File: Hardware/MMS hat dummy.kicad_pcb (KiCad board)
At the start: 2 copper layers, 100 x 20 mm, 26 parts, among them J1 Chainbus in, J2 Chainbus Out, U1 XC6206P332MR

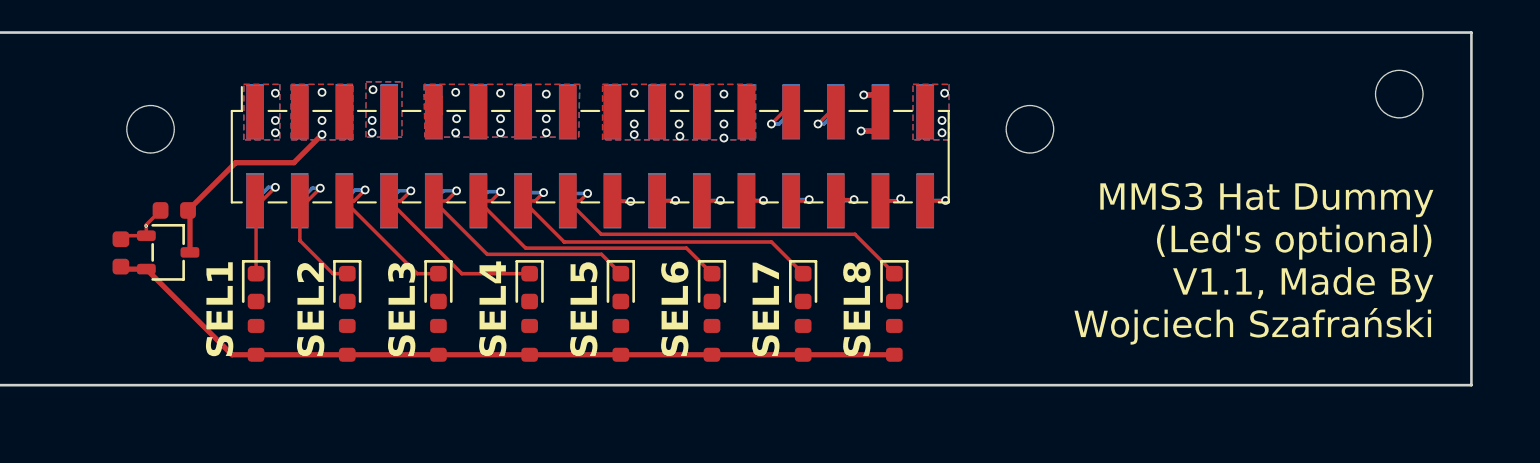
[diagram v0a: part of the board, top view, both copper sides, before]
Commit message: MAJOR - fixed DIN holes misalignment
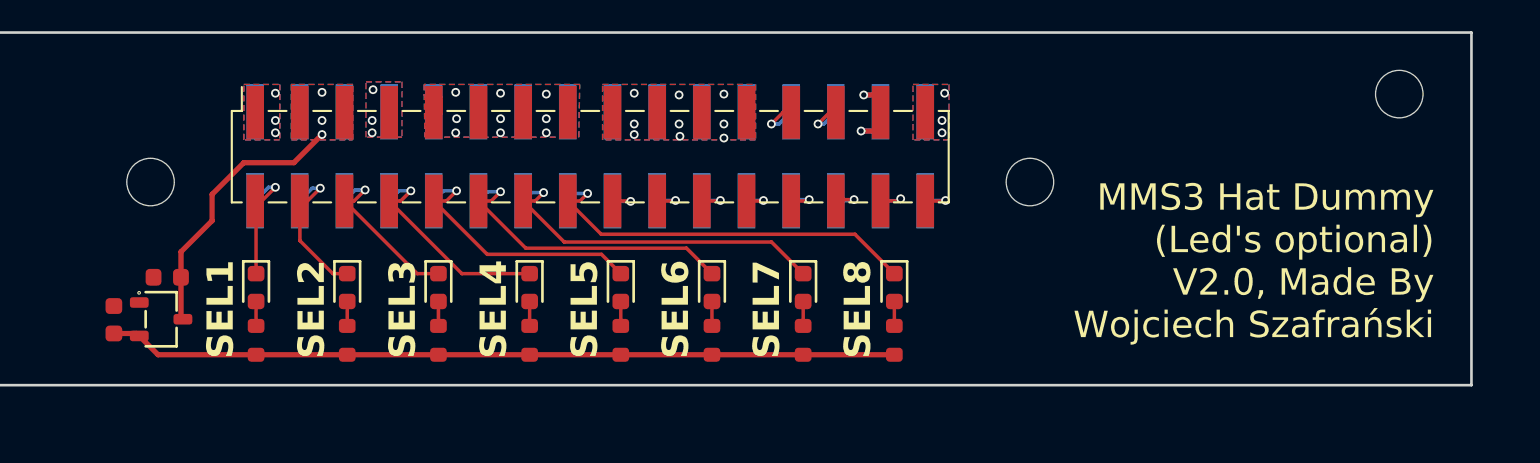
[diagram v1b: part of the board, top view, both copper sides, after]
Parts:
- moved C1 3.82 mm to (104.0, 102.4)
- moved C2 3.82 mm to (100.9, 104.8)
- moved U1 3.82 mm to (103.6, 104.8)
- moved H5 3.00 mm to (103.0, 97.0)
- moved H6 3.00 mm to (153.0, 97.0)
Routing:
- net +5V: track 11.8 -> 15.5 mm
- net GND: track 3.30 -> 0.00 mm
- net Net-(D8-Pad2): track 0.00 -> 1.39 mm
- net Net-(D7-Pad2): track 0.00 -> 1.39 mm
- net Net-(D6-Pad2): track 0.00 -> 1.39 mm
- net Net-(D5-Pad2): track 0.00 -> 1.39 mm
- net Net-(D4-Pad2): track 0.00 -> 1.39 mm
- net Net-(D3-Pad2): track 0.00 -> 1.39 mm
- net Net-(D2-Pad2): track 0.00 -> 1.39 mm
- net Net-(D1-Pad2): track 0.00 -> 1.39 mm
- net +3V3: track 46.1 -> 44.9 mm
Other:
- board text added: "MMS3 Hat Dummy (Led's optional) V2.0, Made By Wojciech Szafrański"
- board text removed: "MMS3 Hat Dummy (Led's optional) V1.1, Made By Wojciech Szafrański"
- board text removed: "i"
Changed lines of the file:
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@@
 	(title_block
 		(title "MMS hat dummy")
-		(date "2026-06-23")
-		(rev "Ver 1.0")
+		(date "2026-10-19")
+		(rev "2.0")
 		(comment 1 "Made by Wojciech Szafrański")
 		(comment 2 "Designed in poland")
@@
 	(footprint "PCM_JLCPCB:C_0603"
 		(layer "F.Cu")
-		(at 104.35 98.615 180)
+		(at 103.95 102.415 180)
 		(descr "Capacitor SMD 0603 (1608 Metric), square (rectangular) end terminal, IPC_7351 nominal, (Body size source: IPC-SM-782 page 76, https://www.pcb-3d.com/wordpress/wp-content/uploads/ipc-sm-782a_amendment_1_and_2.pdf), generated with kicad-footprint-generator")
 		(tags "capacitor")
@@
 	(footprint "PCM_JLCPCB:SOT-23-3_L2.9-W1.6-P1.90-LS2.8-BR"
 		(layer "F.Cu")
-		(at 104 101 180)
+		(at 103.6 104.8 180)
 		(descr "SOT-23-3_L2.9-W1.6-P1.90-LS2.8-BR footprint")
 		(tags "SOT-23-3_L2.9-W1.6-P1.90-LS2.8-BR footprint C2829399")
@@
 		(locked yes)
 		(layer "F.Cu")
-		(at 153 94)
+		(at 153 97)
 		(descr "Mounting Hole 2.7mm, M2.5, no annular, generated by kicad-footprint-generator mountinghole.py")
 		(tags "mountinghole M2.5")
@@
 		(locked yes)
 		(layer "F.Cu")
-		(at 103 94)
+		(at 103 97)
 		(descr "Mounting Hole 2.7mm, M2.5, no annular, generated by kicad-footprint-generator mountinghole.py")
 		(tags "mountinghole M2.5")
@@
 	(footprint "PCM_JLCPCB:C_0603"
 		(layer "F.Cu")
-		(at 101.314826 101.030476 90)
+		(at 100.914826 104.830476 90)
 		(descr "Capacitor SMD 0603 (1608 Metric), square (rectangular) end terminal, IPC_7351 nominal, (Body size source: IPC-SM-782 page 76, https://www.pcb-3d.com/wordpress/wp-content/uploads/ipc-sm-782a_amendment_1_and_2.pdf), generated with kicad-footprint-generator")
 		(tags "capacitor")
@@
 		(layer "Edge.Cuts")
 	)
-	(gr_text "MMS3 Hat Dummy\n(Led's optional)\nV1.1, Made By\nWojciech Szafrański"
+	(gr_text "MMS3 Hat Dummy\n(Led's optional)\nV2.0, Made By\nWojciech Szafrański"
 		(at 176 106 0)
 		(layer "F.SilkS")
@@
 		)
 	)
-	(gr_text "i"
-		(at 157.776979 93.689038 0)
-		(layer "B.SilkS")
-		(effects
-			(font
-				(face "Microsoft Himalaya")
-				(size 3 3)
-				(thickness 0.4)
-				(bold yes)
-			)
-			(justify left bottom mirror)
-		)
-		(render_cache "i" 0
-			(polygon
-				(pts
-					(xy 157.147015 89.982876) (xy 157.015354 89.999715) (xy 156.905581 90.048088) (xy 156.851273 90.100029)
-					(xy 156.816027 90.1784) (xy 156.802633 90.293553) (xy 156.815759 90.403246) (xy 156.850792 90.48016)
-					(xy 156.905581 90.533155) (xy 157.015476 90.582921) (xy 157.147015 90.600199) (xy 157.281779 90.58274)
-					(xy 157.390647 90.533155) (xy 157.444135 90.480351) (xy 157.478493 90.403468) (xy 157.491398 90.293553)
-					(xy 157.478227 90.178165) (xy 157.44366 90.099831) (xy 157.390647 90.048088) (xy 157.281907 89.999893)
-				)
-			)
-			(polygon
-				(pts
-					(xy 156.831942 90.88578) (xy 156.831942 93.179038) (xy 157.466118 93.179038) (xy 157.466118 90.88578)
-				)
-			)
-		)
-	)
 	(gr_text "Front and Back keepout\nzone for DIN rail mount"
 		(locked yes)
@@
 	(dimension
 		(type orthogonal)
-		(locked yes)
 		(layer "User.1")
 		(pts
-			(xy 153 94) (xy 178 88)
+			(xy 153 97) (xy 178 88)
 		)
 		(height 34)
@@
 			(keep_text_aligned yes)
 		)
-		(gr_text "6"
-			(locked yes)
-			(at 185.85 91 90)
+		(gr_text "9"
+			(at 185.85 92.5 90)
 			(layer "User.1")
 			(effects
@@
 	)
 	(segment
-		(start 102.76 101.95)
-		(end 101.45435 101.95)
+		(start 109 106.82)
+		(end 103.43 106.82)
 		(width 0.3)
 		(layer "F.Cu")
@@
 	)
 	(segment
-		(start 107.63 106.82)
-		(end 102.76 101.95)
+		(start 109 106.82)
+		(end 145.29 106.82)
 		(width 0.3)
 		(layer "F.Cu")
@@
 	)
 	(segment
-		(start 101.45435 101.95)
-		(end 101.314826 101.810476)
+		(start 100.914826 105.610476)
+		(end 102.220476 105.610476)
 		(width 0.3)
 		(layer "F.Cu")
@@
 	)
 	(segment
-		(start 107.63 106.82)
-		(end 145.29 106.82)
+		(start 102.220476 105.610476)
+		(end 102.36 105.75)
+		(width 0.3)
+		(layer "F.Cu")
+		(net "+3V3")
+	)
+	(segment
+		(start 103.43 106.82)
+		(end 102.36 105.75)
 		(width 0.3)
 		(layer "F.Cu")
@@
 	)
 	(segment
+		(start 119.368571 105.18)
+		(end 119.368571 103.79)
+		(width 0.2)
+		(layer "F.Cu")
+		(net "Net-(D3-Pad2)")
+	)
+	(segment
+		(start 124.552857 105.18)
+		(end 124.552857 103.79)
+		(width 0.2)
+		(layer "F.Cu")
+		(net "Net-(D4-Pad2)")
+	)
+	(segment
 		(start 109 98.128272)
 		(end 108.95 98.078272)
@@
 	)
 	(segment
-		(start 105.13 98.615)
-		(end 107.845 95.9)
+		(start 109 105.18)
+		(end 109 103.79)
+		(width 0.2)
+		(layer "F.Cu")
+		(net "Net-(D1-Pad2)")
+	)
+	(segment
+		(start 104.73 102.415)
+		(end 104.73 104.69)
+		(width 0.3)
+		(layer "F.Cu")
+		(net "+5V")
+	)
+	(segment
+		(start 104.73 104.69)
+		(end 104.84 104.8)
+		(width 0.3)
+		(layer "F.Cu")
+		(net "+5V")
+	)
+	(segment
+		(start 104.73 102.415)
+		(end 104.73 100.97)
+		(width 0.3)
+		(layer "F.Cu")
+		(net "+5V")
+	)
+	(segment
+		(start 106.5 99.2)
+		(end 106.5 97.7)
 		(width 0.3)
 		(layer "F.Cu")
@@
 	)
 	(segment
-		(start 107.845 95.9)
-		(end 111.15 95.9)
+		(start 104.73 100.97)
+		(end 106.5 99.2)
 		(width 0.3)
 		(layer "F.Cu")
@@
 	)
 	(segment
-		(start 105.24 98.725)
-		(end 105.13 98.615)
+		(start 106.5 97.7)
+		(end 108.3 95.9)
 		(width 0.3)
 		(layer "F.Cu")
@@
 	)
 	(segment
-		(start 105.24 101)
-		(end 105.24 98.725)
+		(start 108.3 95.9)
+		(end 111.15 95.9)
 		(width 0.3)
 		(layer "F.Cu")
@@
 		(net "+5V")
 	)
-	(segment
-		(start 102.76 100.05)
-		(end 101.515302 100.05)
-		(width 0.2)
-		(layer "F.Cu")
-		(net "GND")
-	)
-	(segment
-		(start 101.515302 100.05)
-		(end 101.314826 100.250476)
-		(width 0.2)
-		(layer "F.Cu")
-		(net "GND")
-	)
-	(segment
-		(start 102.76 99.425)
-		(end 103.57 98.615)
-		(width 0.2)
-		(layer "F.Cu")
-		(net "GND")
-	)
-	(segment
-		(start 102.76 100.05)
-		(end 102.76 99.425)
-		(width 0.2)
-		(layer "F.Cu")
-		(net "GND")
-	)
 	(via
 		(at 133.05 92.05)
@@
 		(net "/Chainbus.RX")
 	)
+	(segment
+		(start 129.737143 103.79)
+		(end 129.737143 105.18)
+		(width 0.2)
+		(layer "F.Cu")
+		(net "Net-(D5-Pad2)")
+	)
+	(segment
+		(start 145.29 105.18)
+		(end 145.29 103.79)
+		(width 0.2)
+		(layer "F.Cu")
+		(net "Net-(D8-Pad2)")
+	)
+	(segment
+		(start 140.105714 103.79)
+		(end 140.105714 105.18)
+		(width 0.2)
+		(layer "F.Cu")
+		(net "Net-(D7-Pad2)")
+	)
+	(segment
+		(start 134.921429 105.18)
+		(end 134.921429 103.79)
+		(width 0.2)
+		(layer "F.Cu")
+		(net "Net-(D6-Pad2)")
+	)
+	(segment
+		(start 114.184286 103.79)
+		(end 114.184286 105.18)
+		(width 0.2)
+		(layer "F.Cu")
+		(net "Net-(D2-Pad2)")
+	)
 	(zone
